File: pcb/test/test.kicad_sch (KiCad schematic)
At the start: 16 parts, among them IC1 ADG904BRUZ-REEL7, J1 CONSMA013.062-G, J3 Conn_01x04, U2 TL081

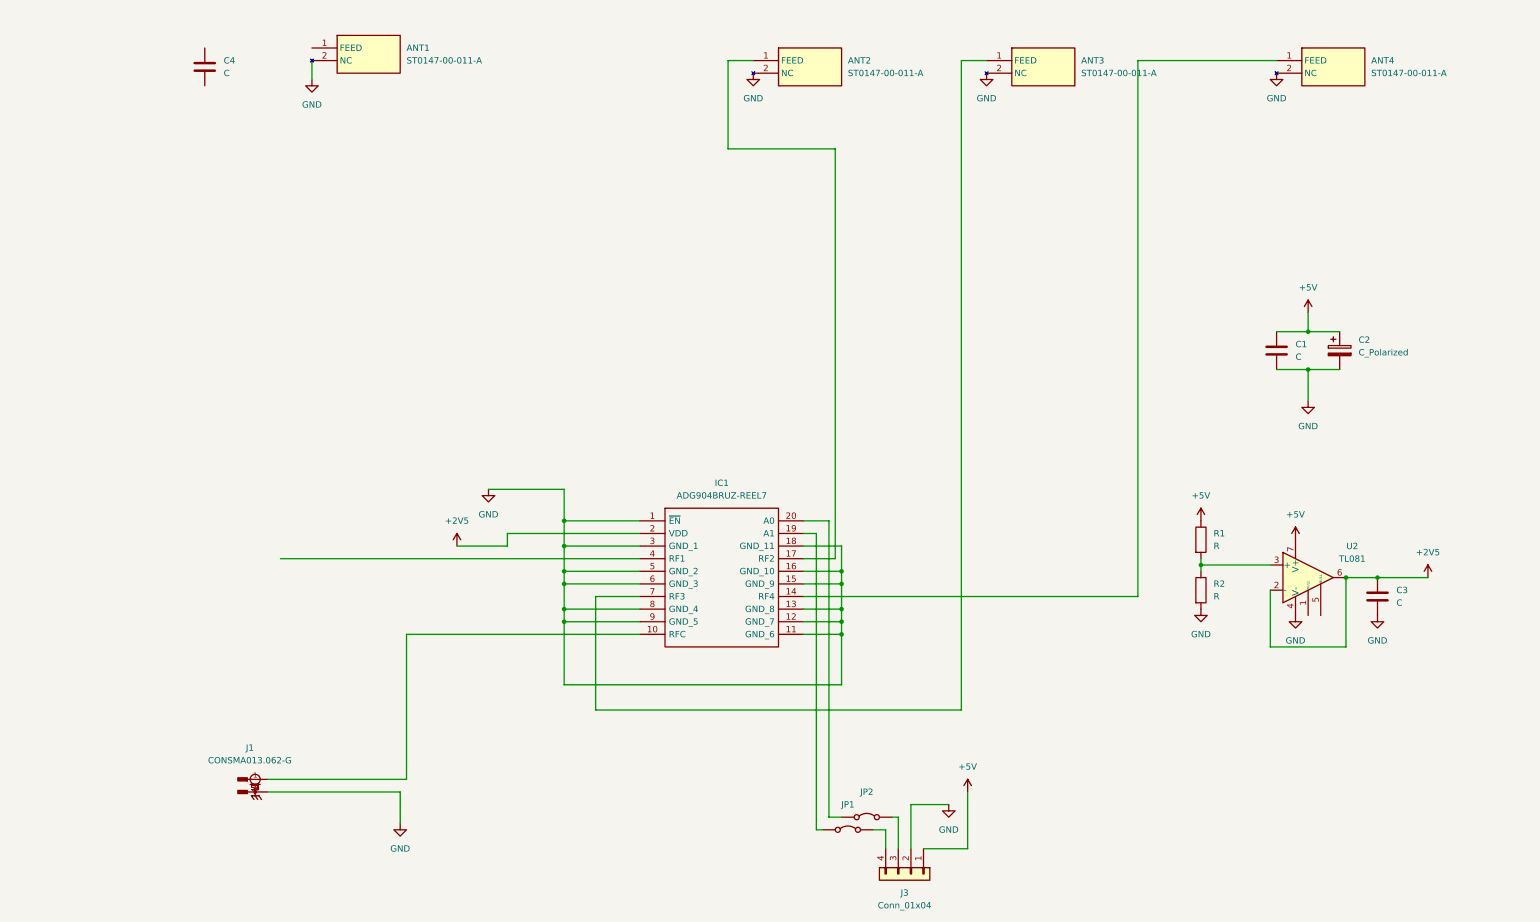
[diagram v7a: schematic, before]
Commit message: circuit adaptation impédance
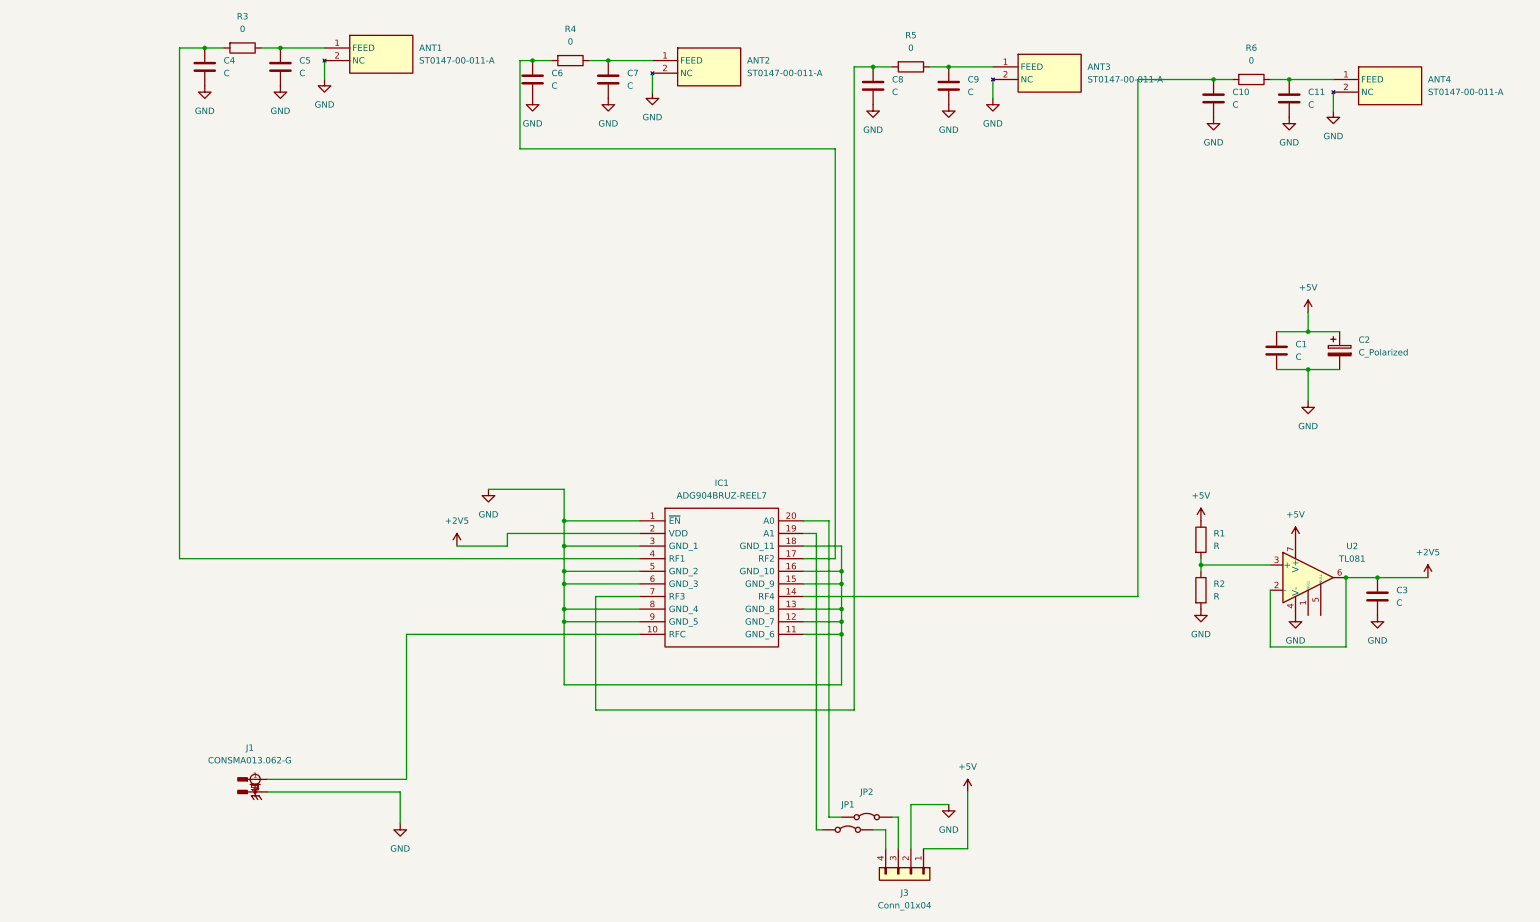
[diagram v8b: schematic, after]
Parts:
- added C10, C11, C5, C6, C7, C8, C9: C, Capacitor_SMD:C_0201_0603Metric, symbol Device:C
- added R3, R4, R5, R6: 0, Resistor_SMD:R_0201_0603Metric, symbol Device:R
- C4: footprint (none) -> Capacitor_SMD:C_0201_0603Metric
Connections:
- net GND: now also C4.2, C10.2, C11.2, C5.2, C6.2, C7.2, C8.2, C9.2
- net at ANT3.1 (FEED): now also C9.1, R5.1; no longer IC1.7 (RF3)
- net at C4.1: now also IC1.4 (RF1), R3.2
- net at IC1.14 (RF4): now also C10.1, R6.2; no longer ANT4.1 (FEED)
- net at ANT2.1 (FEED): now also C7.1, R4.1; no longer IC1.17 (RF2)
- net at ANT1.1 (FEED): now also C5.1, R3.1
- new net: C8.1, IC1.7 (RF3), R5.2
- new net: C6.1, IC1.17 (RF2), R4.2
- new net: ANT4.1 (FEED), C11.1, R6.1
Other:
- moved on the sheet: ANT1
